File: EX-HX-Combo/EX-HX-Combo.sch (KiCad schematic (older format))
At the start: 41 parts, among them CN1 DB9 Male, J1 IDE_CONNECTOR, J200 Bus_Tandy_Plus_Through, J3 Bus_Tandy_Plus, SW1 SW_DIP_x10, U1 BIOS FLASH, U2 74HCT245, U3 1.8432 MHz, U4 DS1315, U5 AS6C4008-55PCN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

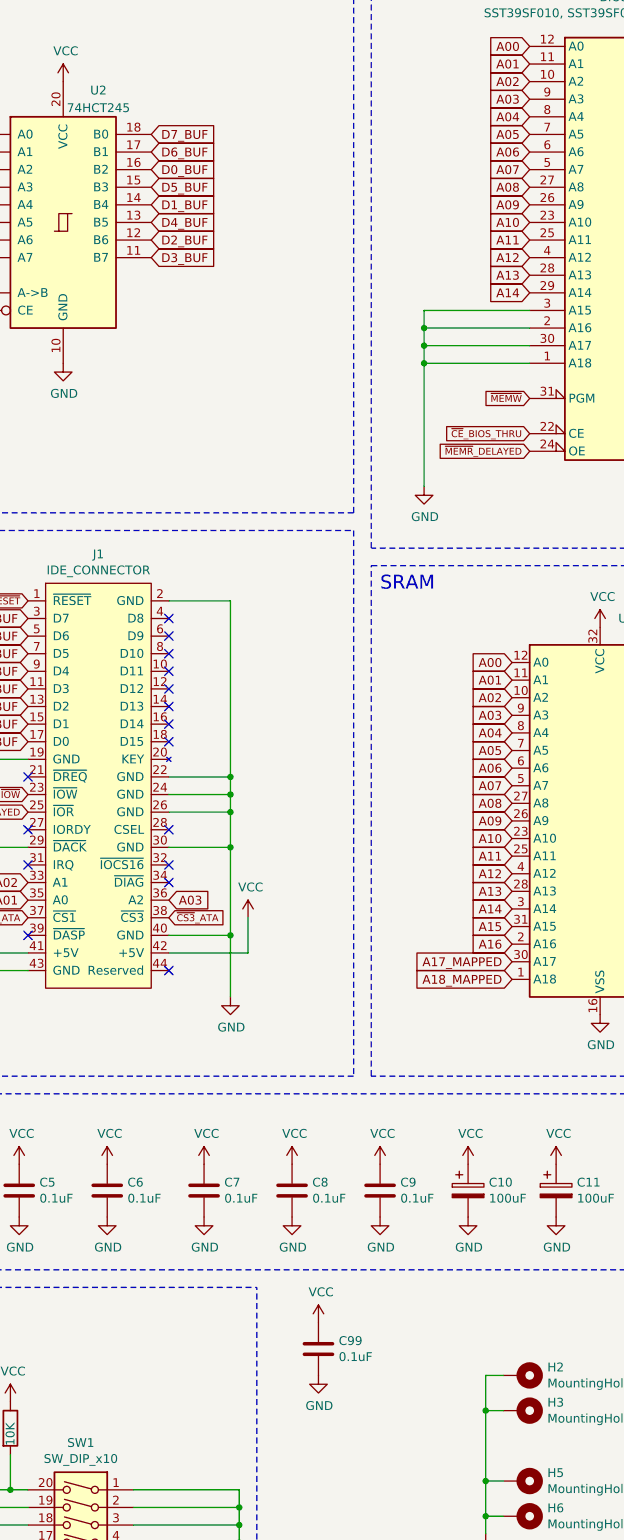
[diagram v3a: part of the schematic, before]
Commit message: EX-HX-Combo layout work: All connections have been made, in progress on tidy up.
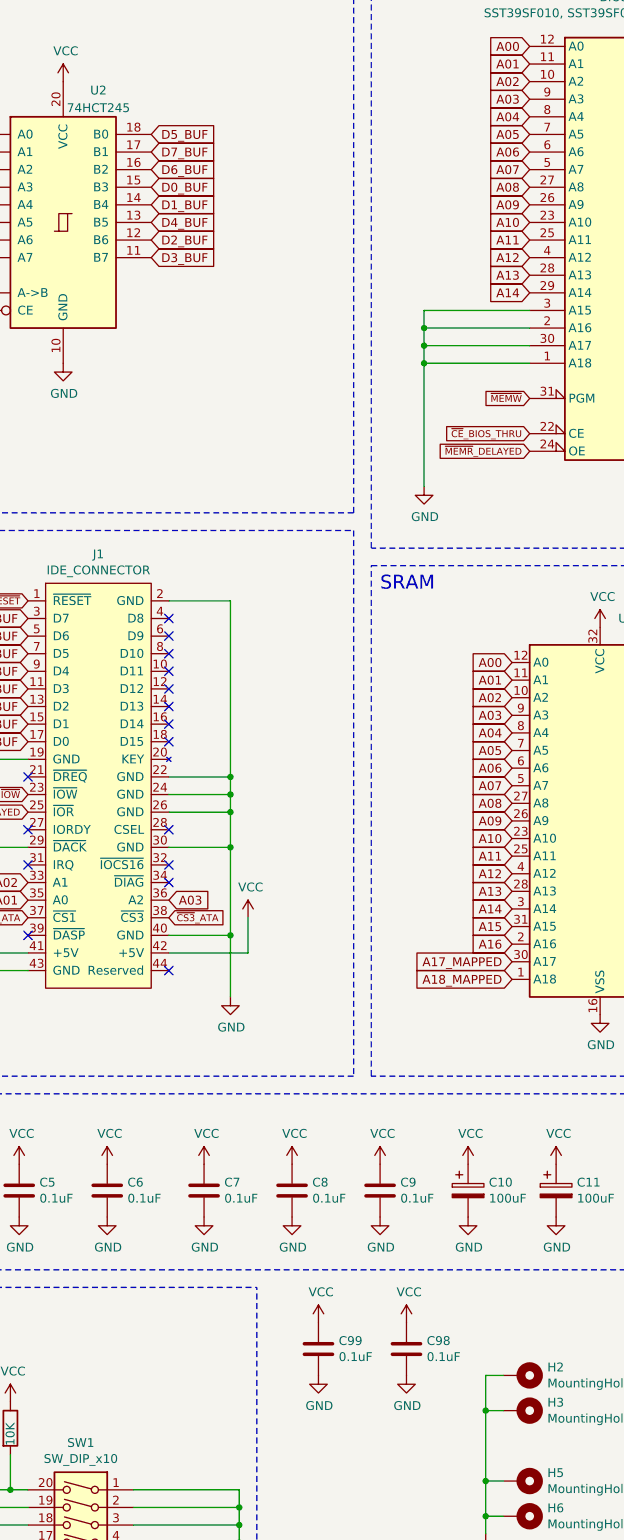
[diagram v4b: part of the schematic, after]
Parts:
- added C98: 0.1uF, Capacitor_SMD:C_1206_3216Metric, symbol Device:C
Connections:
- net D0_BUF: now also U2.15 (B3); no longer U2.16 (B2)
- net D5_BUF: now also U2.18 (B0); no longer U2.15 (B3)
- net D6_BUF: now also U2.16 (B2); no longer U2.17 (B1)
- net D7_BUF: now also U2.17 (B1); no longer U2.18 (B0)
- net GND: now also C98.2
- net VCC: now also C98.1
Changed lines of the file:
@@
 Wire Wire Line
 	11050 10100 11100 10100
+Text GLabel 11100 1800 2    50   Input ~ 0
+D7_BUF
+Text GLabel 11100 1900 2    50   Input ~ 0
+D6_BUF
 Text GLabel 11100 1700 2    50   Input ~ 0
-D7_BUF
-Text GLabel 11100 1800 2    50   Input ~ 0
-D6_BUF
-Text GLabel 11100 2000 2    50   Input ~ 0
 D5_BUF
 Text GLabel 11100 2200 2    50   Input ~ 0
@@
 Text GLabel 9000 9900 0    50   Input ~ 0
 UART_S0
-Text GLabel 11100 1900 2    50   Input ~ 0
+Text GLabel 11100 2000 2    50   Input ~ 0
 D0_BUF
 Text GLabel 11100 2100 2    50   Input ~ 0
@@
 	1    0    0    -1
 $EndComp
+$Comp
+L Device:C C98
+U 1 1 6143E0B4
+P 12550 8600
+F 0 "C98" H 12665 8646 50  0000 L CNN
+F 1 "0.1uF" H 12665 8555 50  0000 L CNN
+F 2 "Capacitor_SMD:C_1206_3216Metric" H 12588 8450 50  0001 C CNN
+F 3 "~" H 12550 8600 50  0001 C CNN
+	1    12550 8600
+	1    0    0    -1
+$EndComp
+$Comp
+L power:GND #PWR?
+U 1 1 6143EB1E
+P 12550 8750
+F 0 "#PWR?" H 12550 8500 50  0001 C CNN
+F 1 "GND" H 12555 8577 50  0000 C CNN
+F 2 "" H 12550 8750 50  0001 C CNN
+F 3 "" H 12550 8750 50  0001 C CNN
+	1    12550 8750
+	1    0    0    -1
+$EndComp
+$Comp
+L power:VCC #PWR?
+U 1 1 6143EB28
+P 12550 8450
+F 0 "#PWR?" H 12550 8300 50  0001 C CNN
+F 1 "VCC" H 12565 8623 50  0000 C CNN
+F 2 "" H 12550 8450 50  0001 C CNN
+F 3 "" H 12550 8450 50  0001 C CNN
+	1    12550 8450
+	1    0    0    -1
+$EndComp

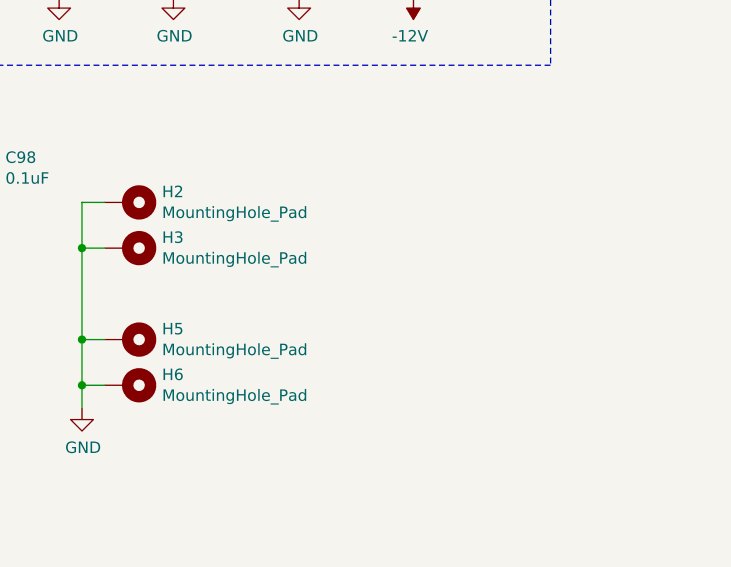
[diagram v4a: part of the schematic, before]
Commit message: Add alignment holes to EX-HX-Combo.
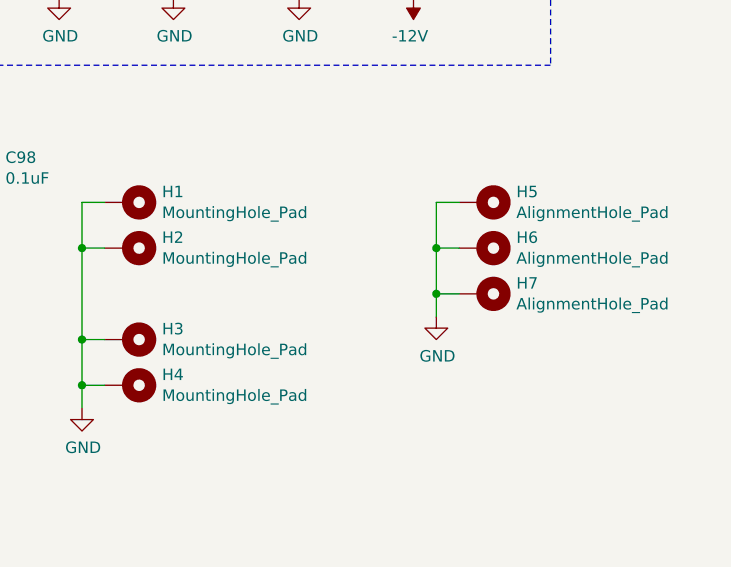
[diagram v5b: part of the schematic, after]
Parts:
- added H5, H6, H7: AlignmentHole_Pad, 00Custom:AlignmentHole, symbol Mechanical:MountingHole_Pad
- renumbered H2 to H1, H3 to H2, H5 to H3, H6 to H4
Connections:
- net GND: now also H5.1, H6.1, H7.1
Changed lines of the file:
@@
 $EndComp
 $Comp
-L Mechanical:MountingHole_Pad H2
+L Mechanical:MountingHole_Pad H1
 U 1 1 60D6AC46
 P 13200 8750
-F 0 "H2" V 13154 8900 50  0000 L CNN
+F 0 "H1" V 13154 8900 50  0000 L CNN
 F 1 "MountingHole_Pad" V 13245 8900 50  0000 L CNN
 F 2 "MountingHole:MountingHole_3.5mm_Pad" H 13200 8750 50  0001 C CNN
@@
 $EndComp
 $Comp
-L Mechanical:MountingHole_Pad H3
+L Mechanical:MountingHole_Pad H2
 U 1 1 60D6B05B
 P 13200 8950
-F 0 "H3" V 13154 9100 50  0000 L CNN
+F 0 "H2" V 13154 9100 50  0000 L CNN
 F 1 "MountingHole_Pad" V 13245 9100 50  0000 L CNN
 F 2 "MountingHole:MountingHole_3.5mm_Pad" H 13200 8950 50  0001 C CNN
@@
 $EndComp
 $Comp
-L Mechanical:MountingHole_Pad H5
+L Mechanical:MountingHole_Pad H3
 U 1 1 60D6B4F1
 P 13200 9350
-F 0 "H5" V 13154 9500 50  0000 L CNN
+F 0 "H3" V 13154 9500 50  0000 L CNN
 F 1 "MountingHole_Pad" V 13245 9500 50  0000 L CNN
 F 2 "MountingHole:MountingHole_3.5mm_Pad" H 13200 9350 50  0001 C CNN
@@
 	13000 9350 13000 9550
 $Comp
-L Mechanical:MountingHole_Pad H6
+L Mechanical:MountingHole_Pad H4
 U 1 1 60D9AE58
 P 13200 9550
-F 0 "H6" V 13154 9700 50  0000 L CNN
+F 0 "H4" V 13154 9700 50  0000 L CNN
 F 1 "MountingHole_Pad" V 13245 9700 50  0000 L CNN
 F 2 "MountingHole:MountingHole_3.5mm_Pad" H 13200 9550 50  0001 C CNN
@@
 $EndComp
 $Comp
-L power:GND #PWR?
+L power:GND #PWR0177
 U 1 1 6143EB1E
 P 12550 8750
-F 0 "#PWR?" H 12550 8500 50  0001 C CNN
+F 0 "#PWR0177" H 12550 8500 50  0001 C CNN
 F 1 "GND" H 12555 8577 50  0000 C CNN
 F 2 "" H 12550 8750 50  0001 C CNN
@@
 $EndComp
 $Comp
-L power:VCC #PWR?
+L power:VCC #PWR0178
 U 1 1 6143EB28
 P 12550 8450
-F 0 "#PWR?" H 12550 8300 50  0001 C CNN
+F 0 "#PWR0178" H 12550 8300 50  0001 C CNN
 F 1 "VCC" H 12565 8623 50  0000 C CNN
 F 2 "" H 12550 8450 50  0001 C CNN
@@
 	1    0    0    -1
 $EndComp
+$Comp
+L Mechanical:MountingHole_Pad H5
+U 1 1 61187FCA
+P 14750 8750
+F 0 "H5" V 14704 8900 50  0000 L CNN
+F 1 "AlignmentHole_Pad" V 14795 8900 50  0000 L CNN
+F 2 "00Custom:AlignmentHole" H 14750 8750 50  0001 C CNN
+F 3 "~" H 14750 8750 50  0001 C CNN
+	1    14750 8750
+	0    1    1    0
+$EndComp
+$Comp
+L Mechanical:MountingHole_Pad H6
+U 1 1 611A4105
+P 14750 8950
+F 0 "H6" V 14704 9100 50  0000 L CNN
+F 1 "AlignmentHole_Pad" V 14795 9100 50  0000 L CNN
+F 2 "00Custom:AlignmentHole" H 14750 8950 50  0001 C CNN
+F 3 "~" H 14750 8950 50  0001 C CNN
+	1    14750 8950
+	0    1    1    0
+$EndComp
+$Comp
+L Mechanical:MountingHole_Pad H7
+U 1 1 611C6C9E
+P 14750 9150
+F 0 "H7" V 14704 9300 50  0000 L CNN
+F 1 "AlignmentHole_Pad" V 14795 9300 50  0000 L CNN
+F 2 "00Custom:AlignmentHole" H 14750 9150 50  0001 C CNN
+F 3 "~" H 14750 9150 50  0001 C CNN
+	1    14750 9150
+	0    1    1    0
+$EndComp
+Wire Wire Line
+	14650 8750 14550 8750
+Wire Wire Line
+	14550 8750 14550 8950
+$Comp
+L power:GND #PWR0179
+U 1 1 6120C5C6
+P 14550 9250
+F 0 "#PWR0179" H 14550 9000 50  0001 C CNN
+F 1 "GND" H 14555 9077 50  0000 C CNN
+F 2 "" H 14550 9250 50  0001 C CNN
+F 3 "" H 14550 9250 50  0001 C CNN
+	1    14550 9250
+	1    0    0    -1
+$EndComp
+Wire Wire Line
+	14650 8950 14550 8950
+Connection ~ 14550 8950
+Wire Wire Line
+	14550 8950 14550 9150
+Wire Wire Line
+	14650 9150 14550 9150
+Connection ~ 14550 9150
+Wire Wire Line
+	14550 9150 14550 9250
 $EndSCHEMATC

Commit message: EX-HX-Combo layout work.
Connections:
- net D0: now also U2.5 (A3); no longer U2.4 (A2)
- net D5: now also U2.2 (A0); no longer U2.5 (A3)
- net D6: now also U2.4 (A2); no longer U2.3 (A1)
- net D7: now also U2.3 (A1); no longer U2.2 (A0)
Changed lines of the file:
@@
 Text GLabel 11100 2400 2    50   Input ~ 0
 D3_BUF
-Text GLabel 10100 1900 0    50   Input ~ 0
+Text GLabel 10100 2000 0    50   Input ~ 0
 D0
 Text GLabel 10100 2100 0    50   Input ~ 0
@@
 Text GLabel 10100 2200 0    50   Input ~ 0
 D4
-Text GLabel 10100 2000 0    50   Input ~ 0
+Text GLabel 10100 1700 0    50   Input ~ 0
 D5
+Text GLabel 10100 1900 0    50   Input ~ 0
+D6
 Text GLabel 10100 1800 0    50   Input ~ 0
-D6
-Text GLabel 10100 1700 0    50   Input ~ 0
 D7
 Text Notes 2350 11050 0    50   ~ 0

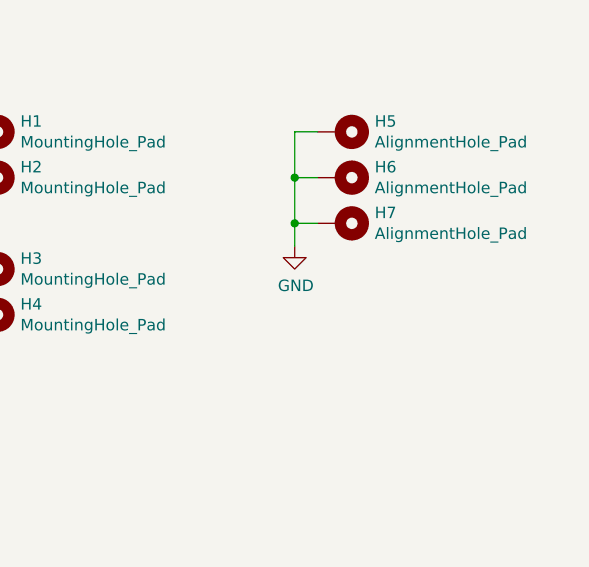
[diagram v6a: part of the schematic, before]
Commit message: EX-HX-Combo layout work, including hole for DB-9 connector.
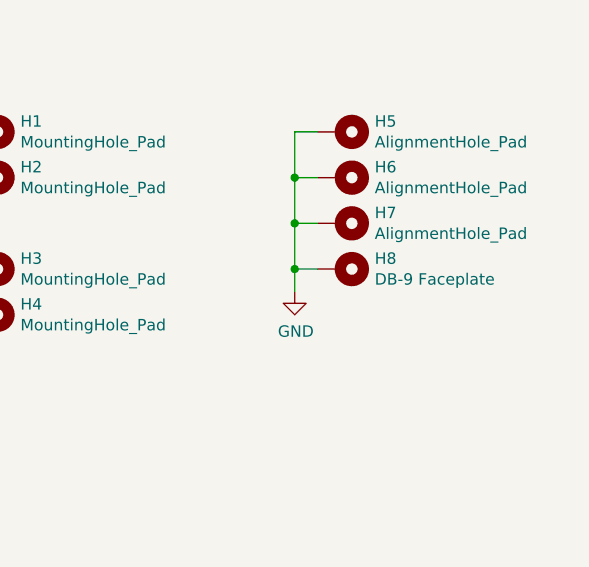
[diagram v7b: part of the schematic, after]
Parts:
- added H8: DB-9 Faceplate, 00Custom:DB9_Face, symbol Mechanical:MountingHole_Pad
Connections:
- net GND: now also H8.1
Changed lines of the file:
@@
 L power:GND #PWR0179
 U 1 1 6120C5C6
-P 14550 9250
-F 0 "#PWR0179" H 14550 9000 50  0001 C CNN
-F 1 "GND" H 14555 9077 50  0000 C CNN
-F 2 "" H 14550 9250 50  0001 C CNN
-F 3 "" H 14550 9250 50  0001 C CNN
-	1    14550 9250
+P 14550 9450
+F 0 "#PWR0179" H 14550 9200 50  0001 C CNN
+F 1 "GND" H 14555 9277 50  0000 C CNN
+F 2 "" H 14550 9450 50  0001 C CNN
+F 3 "" H 14550 9450 50  0001 C CNN
+	1    14550 9450
 	1    0    0    -1
 $EndComp
@@
 	14650 9150 14550 9150
 Connection ~ 14550 9150
+$Comp
+L Mechanical:MountingHole_Pad H8
+U 1 1 611975A0
+P 14750 9350
+F 0 "H8" V 14704 9500 50  0000 L CNN
+F 1 "DB-9 Faceplate" V 14795 9500 50  0000 L CNN
+F 2 "00Custom:DB9_Face" H 14750 9350 50  0001 C CNN
+F 3 "~" H 14750 9350 50  0001 C CNN
+	1    14750 9350
+	0    1    1    0
+$EndComp
 Wire Wire Line
-	14550 9150 14550 9250
+	14550 9150 14550 9350
+Wire Wire Line
+	14650 9350 14550 9350
+Connection ~ 14550 9350
+Wire Wire Line
+	14550 9350 14550 9450
 $EndSCHEMATC
